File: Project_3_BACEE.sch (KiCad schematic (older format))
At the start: 16 parts

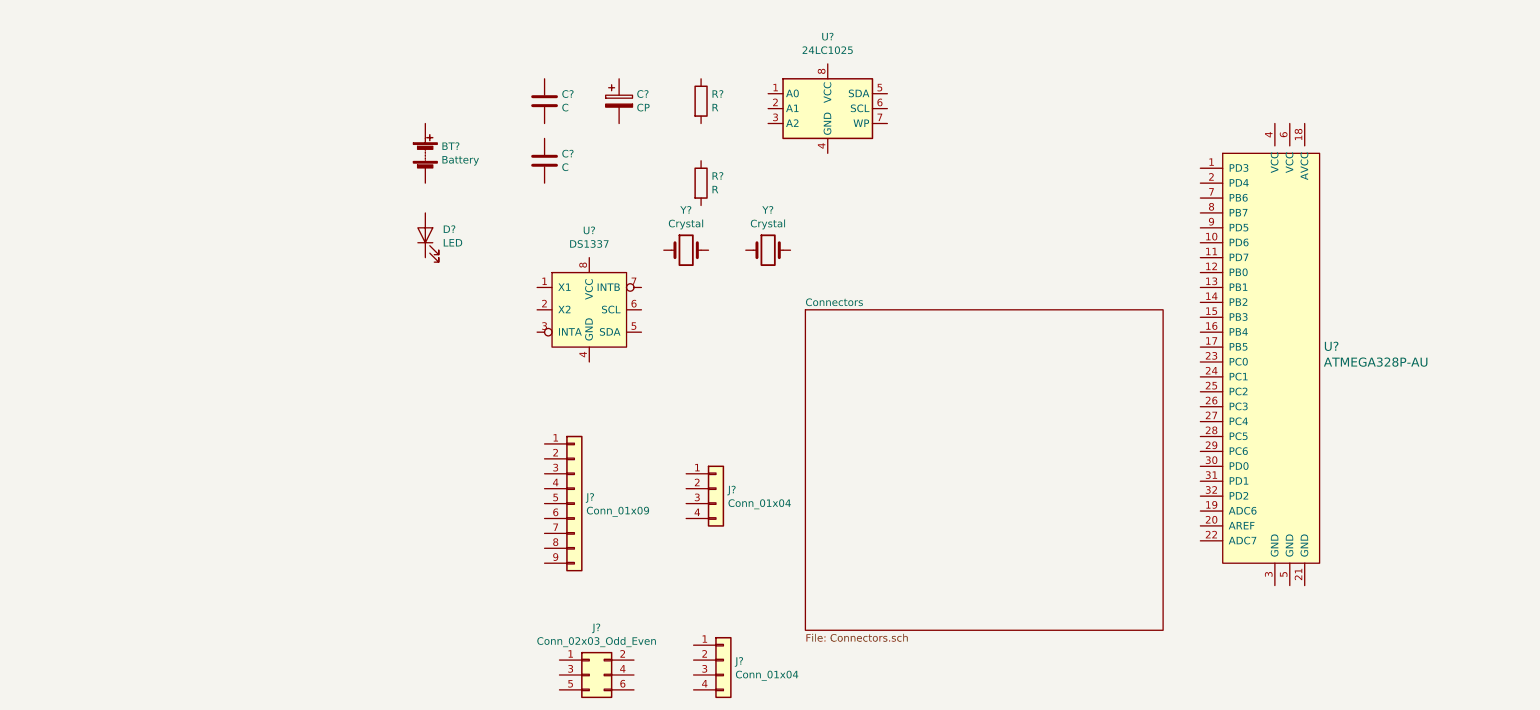
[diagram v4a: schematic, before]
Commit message: Arranged symbols.
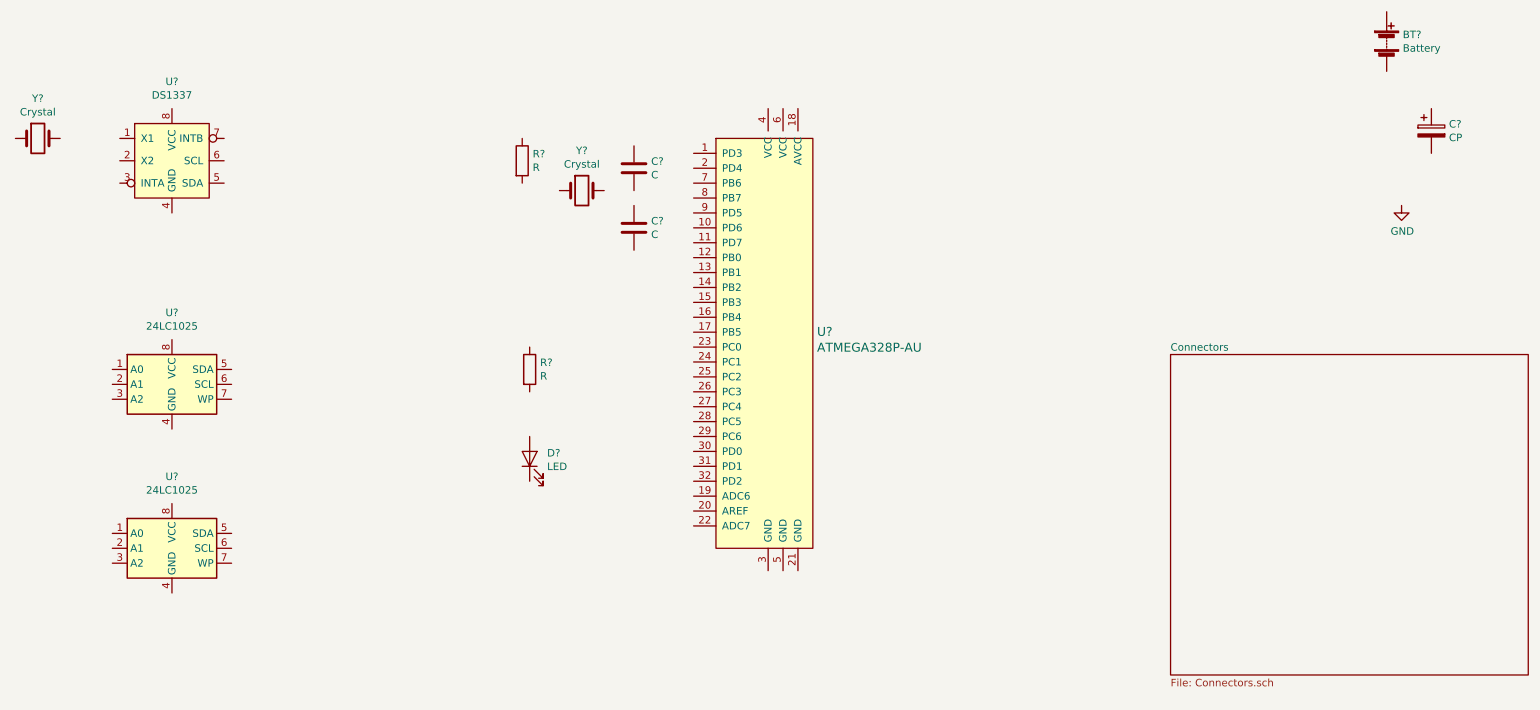
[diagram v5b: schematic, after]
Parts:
- removed J?: Conn_01x09, symbol Connector_Generic:Conn_01x09
- removed J? (x2): Conn_01x04, symbol Connector_Generic:Conn_01x04
- removed J?: Conn_02x03_Odd_Even, symbol Connector_Generic:Conn_02x03_Odd_Even
- added U?: 24LC1025, symbol Memory_EEPROM:24LC1025
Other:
- moved on the sheet: BT?, C?, D?, R?, U?, Y?
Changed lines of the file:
@@
 L Device:Battery BT?
 U 1 1 5D8368FA
-P 3700 2550
-F 0 "BT?" H 3808 2596 50  0000 L CNN
-F 1 "Battery" H 3808 2505 50  0000 L CNN
-F 2 "" V 3700 2610 50  0001 C CNN
-F 3 "~" V 3700 2610 50  0001 C CNN
-	1    3700 2550
+P 10150 1800
+F 0 "BT?" H 10258 1846 50  0000 L CNN
+F 1 "Battery" H 10258 1755 50  0000 L CNN
+F 2 "" V 10150 1860 50  0001 C CNN
+F 3 "~" V 10150 1860 50  0001 C CNN
+	1    10150 1800
 	1    0    0    -1
 $EndComp
@@
 L Device:C C?
 U 1 1 5D837139
-P 4500 2200
-F 0 "C?" H 4615 2246 50  0000 L CNN
-F 1 "C" H 4615 2155 50  0000 L CNN
-F 2 "" H 4538 2050 50  0001 C CNN
-F 3 "~" H 4500 2200 50  0001 C CNN
-	1    4500 2200
+P 5100 2650
+F 0 "C?" H 5215 2696 50  0000 L CNN
+F 1 "C" H 5215 2605 50  0000 L CNN
+F 2 "" H 5138 2500 50  0001 C CNN
+F 3 "~" H 5100 2650 50  0001 C CNN
+	1    5100 2650
 	1    0    0    -1
 $EndComp
@@
 L Device:C C?
 U 1 1 5D837758
-P 4500 2600
-F 0 "C?" H 4615 2646 50  0000 L CNN
-F 1 "C" H 4615 2555 50  0000 L CNN
-F 2 "" H 4538 2450 50  0001 C CNN
-F 3 "~" H 4500 2600 50  0001 C CNN
-	1    4500 2600
+P 5100 3050
+F 0 "C?" H 5215 3096 50  0000 L CNN
+F 1 "C" H 5215 3005 50  0000 L CNN
+F 2 "" H 5138 2900 50  0001 C CNN
+F 3 "~" H 5100 3050 50  0001 C CNN
+	1    5100 3050
 	1    0    0    -1
 $EndComp
@@
 L Device:CP C?
 U 1 1 5D837C3D
-P 5000 2200
-F 0 "C?" H 5118 2246 50  0000 L CNN
-F 1 "CP" H 5118 2155 50  0000 L CNN
-F 2 "" H 5038 2050 50  0001 C CNN
-F 3 "~" H 5000 2200 50  0001 C CNN
-	1    5000 2200
+P 10450 2400
+F 0 "C?" H 10568 2446 50  0000 L CNN
+F 1 "CP" H 10568 2355 50  0000 L CNN
+F 2 "" H 10488 2250 50  0001 C CNN
+F 3 "~" H 10450 2400 50  0001 C CNN
+	1    10450 2400
 	1    0    0    -1
 $EndComp
@@
 L Device:LED D?
 U 1 1 5D8380C0
-P 3700 3100
-F 0 "D?" V 3739 2983 50  0000 R CNN
-F 1 "LED" V 3648 2983 50  0000 R CNN
-F 2 "" H 3700 3100 50  0001 C CNN
-F 3 "~" H 3700 3100 50  0001 C CNN
-	1    3700 3100
+P 4400 4600
+F 0 "D?" V 4439 4483 50  0000 R CNN
+F 1 "LED" V 4348 4483 50  0000 R CNN
+F 2 "" H 4400 4600 50  0001 C CNN
+F 3 "~" H 4400 4600 50  0001 C CNN
+	1    4400 4600
 	0    -1   -1   0
 $EndComp
@@
 L Device:R R?
 U 1 1 5D8396B9
-P 5550 2200
-F 0 "R?" H 5620 2246 50  0000 L CNN
-F 1 "R" H 5620 2155 50  0000 L CNN
-F 2 "" V 5480 2200 50  0001 C CNN
-F 3 "~" H 5550 2200 50  0001 C CNN
-	1    5550 2200
+P 4350 2600
+F 0 "R?" H 4420 2646 50  0000 L CNN
+F 1 "R" H 4420 2555 50  0000 L CNN
+F 2 "" V 4280 2600 50  0001 C CNN
+F 3 "~" H 4350 2600 50  0001 C CNN
+	1    4350 2600
 	1    0    0    -1
 $EndComp
@@
 L Device:R R?
 U 1 1 5D839B71
-P 5550 2750
-F 0 "R?" H 5620 2796 50  0000 L CNN
-F 1 "R" H 5620 2705 50  0000 L CNN
-F 2 "" V 5480 2750 50  0001 C CNN
-F 3 "~" H 5550 2750 50  0001 C CNN
-	1    5550 2750
+P 4400 4000
+F 0 "R?" H 4470 4046 50  0000 L CNN
+F 1 "R" H 4470 3955 50  0000 L CNN
+F 2 "" V 4330 4000 50  0001 C CNN
+F 3 "~" H 4400 4000 50  0001 C CNN
+	1    4400 4000
 	1    0    0    -1
 $EndComp
@@
 L Memory_EEPROM:24LC1025 U?
 U 1 1 5D83A291
-P 6400 2250
-F 0 "U?" H 6400 2731 50  0000 C CNN
-F 1 "24LC1025" H 6400 2640 50  0000 C CNN
-F 2 "" H 6400 2250 50  0001 C CNN
-F 3 "http://ww1.microchip.com/downloads/en/DeviceDoc/21941B.pdf" H 6400 2250 50  0001 C CNN
-	1    6400 2250
+P 2000 4100
+F 0 "U?" H 2000 4581 50  0000 C CNN
+F 1 "24LC1025" H 2000 4490 50  0000 C CNN
+F 2 "" H 2000 4100 50  0001 C CNN
+F 3 "http://ww1.microchip.com/downloads/en/DeviceDoc/21941B.pdf" H 2000 4100 50  0001 C CNN
+	1    2000 4100
 	1    0    0    -1
 $EndComp
 $Sheet
-S 6250 3600 2400 2150
+S 8700 3900 2400 2150
 U 5D83B0D5
 F0 "Connectors" 50
@@
 $EndSheet
 $Comp
-L Connector_Generic:Conn_01x09 J?
-U 1 1 5D83BD36
-P 4700 4900
-F 0 "J?" H 4780 4942 50  0000 L CNN
-F 1 "Conn_01x09" H 4780 4851 50  0000 L CNN
-F 2 "" H 4700 4900 50  0001 C CNN
-F 3 "~" H 4700 4900 50  0001 C CNN
-	1    4700 4900
-	1    0    0    -1
-$EndComp
-$Comp
-L Connector_Generic:Conn_01x04 J?
-U 1 1 5D83CD16
-P 5650 4800
-F 0 "J?" H 5730 4792 50  0000 L CNN
-F 1 "Conn_01x04" H 5730 4701 50  0000 L CNN
-F 2 "" H 5650 4800 50  0001 C CNN
-F 3 "~" H 5650 4800 50  0001 C CNN
-	1    5650 4800
-	1    0    0    -1
-$EndComp
-$Comp
-L Connector_Generic:Conn_02x03_Odd_Even J?
-U 1 1 5D83D5F4
-P 4800 6050
-F 0 "J?" H 4850 6367 50  0000 C CNN
-F 1 "Conn_02x03_Odd_Even" H 4850 6276 50  0000 C CNN
-F 2 "" H 4800 6050 50  0001 C CNN
-F 3 "~" H 4800 6050 50  0001 C CNN
-	1    4800 6050
-	1    0    0    -1
-$EndComp
-$Comp
-L Connector_Generic:Conn_01x04 J?
-U 1 1 5D83E499
-P 5700 5950
-F 0 "J?" H 5780 5942 50  0000 L CNN
-F 1 "Conn_01x04" H 5780 5851 50  0000 L CNN
-F 2 "" H 5700 5950 50  0001 C CNN
-F 3 "~" H 5700 5950 50  0001 C CNN
-	1    5700 5950
-	1    0    0    -1
-$EndComp
-$Comp
 L dk_Embedded-Microcontrollers:ATMEGA328P-AU U?
 U 1 1 5D839D67
-P 9400 3950
-F 0 "U?" H 9728 4053 60  0000 L CNN
-F 1 "ATMEGA328P-AU" H 9728 3947 60  0000 L CNN
-F 2 "digikey-footprints:TQFP-32_7x7mm" H 9600 4150 60  0001 L CNN
-F 3 "http://www.microchip.com/mymicrochip/filehandler.aspx?ddocname=en608326" H 9600 4250 60  0001 L CNN
-F 4 "ATMEGA328P-AU-ND" H 9600 4350 60  0001 L CNN "Digi-Key_PN"
-F 5 "ATMEGA328P-AU" H 9600 4450 60  0001 L CNN "MPN"
-F 6 "Integrated Circuits (ICs)" H 9600 4550 60  0001 L CNN "Category"
-F 7 "Embedded - Microcontrollers" H 9600 4650 60  0001 L CNN "Family"
-F 8 "http://www.microchip.com/mymicrochip/filehandler.aspx?ddocname=en608326" H 9600 4750 60  0001 L CNN "DK_Datasheet_Link"
-F 9 "/product-detail/en/microchip-technology/ATMEGA328P-AU/ATMEGA328P-AU-ND/1832260" H 9600 4850 60  0001 L CNN "DK_Detail_Page"
-F 10 "IC MCU 8BIT 32KB FLASH 32TQFP" H 9600 4950 60  0001 L CNN "Description"
-F 11 "Microchip Technology" H 9600 5050 60  0001 L CNN "Manufacturer"
-F 12 "Active" H 9600 5150 60  0001 L CNN "Status"
-	1    9400 3950
+P 6000 3850
+F 0 "U?" H 6328 3953 60  0000 L CNN
+F 1 "ATMEGA328P-AU" H 6328 3847 60  0000 L CNN
+F 2 "digikey-footprints:TQFP-32_7x7mm" H 6200 4050 60  0001 L CNN
+F 3 "http://www.microchip.com/mymicrochip/filehandler.aspx?ddocname=en608326" H 6200 4150 60  0001 L CNN
+F 4 "ATMEGA328P-AU-ND" H 6200 4250 60  0001 L CNN "Digi-Key_PN"
+F 5 "ATMEGA328P-AU" H 6200 4350 60  0001 L CNN "MPN"
+F 6 "Integrated Circuits (ICs)" H 6200 4450 60  0001 L CNN "Category"
+F 7 "Embedded - Microcontrollers" H 6200 4550 60  0001 L CNN "Family"
+F 8 "http://www.microchip.com/mymicrochip/filehandler.aspx?ddocname=en608326" H 6200 4650 60  0001 L CNN "DK_Datasheet_Link"
+F 9 "/product-detail/en/microchip-technology/ATMEGA328P-AU/ATMEGA328P-AU-ND/1832260" H 6200 4750 60  0001 L CNN "DK_Detail_Page"
+F 10 "IC MCU 8BIT 32KB FLASH 32TQFP" H 6200 4850 60  0001 L CNN "Description"
+F 11 "Microchip Technology" H 6200 4950 60  0001 L CNN "Manufacturer"
+F 12 "Active" H 6200 5050 60  0001 L CNN "Status"
+	1    6000 3850
 	1    0    0    -1
 $EndComp
@@
 L Real_Time_Clock:DS1337 U?
 U 1 1 5D83D55D
-P 4800 3600
-F 0 "U?" H 4800 4131 50  0000 C CNN
-F 1 "DS1337" H 4800 4040 50  0000 C CNN
-F 2 "" H 5050 4350 50  0001 C CNN
-F 3 "http://www.farnell.com/datasheets/2000844.pdf?_ga=2.177508589.917776798.1568905288-909876714.1550950510&_gac=1.216414692.1568905288.Cj0KCQjwzozsBRCNARIsAEM9kBOgoySVZbm8O6iFhnJvaEFTPgnKihPjdqZAtUZmWq1n3gbdbDGyVXUaAgFCEALw_wcB" H 5050 4350 50  0001 C CNN
-	1    4800 3600
+P 2000 2600
+F 0 "U?" H 2000 3131 50  0000 C CNN
+F 1 "DS1337" H 2000 3040 50  0000 C CNN
+F 2 "" H 2250 3350 50  0001 C CNN
+F 3 "http://www.farnell.com/datasheets/2000844.pdf?_ga=2.177508589.917776798.1568905288-909876714.1550950510&_gac=1.216414692.1568905288.Cj0KCQjwzozsBRCNARIsAEM9kBOgoySVZbm8O6iFhnJvaEFTPgnKihPjdqZAtUZmWq1n3gbdbDGyVXUaAgFCEALw_wcB" H 2250 3350 50  0001 C CNN
+	1    2000 2600
 	1    0    0    -1
 $EndComp
@@
 L Device:Crystal Y?
 U 1 1 5D83E063
-P 5450 3200
-F 0 "Y?" H 5450 3468 50  0000 C CNN
-F 1 "Crystal" H 5450 3377 50  0000 C CNN
-F 2 "" H 5450 3200 50  0001 C CNN
-F 3 "~" H 5450 3200 50  0001 C CNN
-	1    5450 3200
+P 1100 2450
+F 0 "Y?" H 1100 2718 50  0000 C CNN
+F 1 "Crystal" H 1100 2627 50  0000 C CNN
+F 2 "" H 1100 2450 50  0001 C CNN
+F 3 "~" H 1100 2450 50  0001 C CNN
+	1    1100 2450
 	1    0    0    -1
 $EndComp
@@
 L Device:Crystal Y?
 U 1 1 5D83E859
-P 6000 3200
-F 0 "Y?" H 6000 3468 50  0000 C CNN
-F 1 "Crystal" H 6000 3377 50  0000 C CNN
-F 2 "" H 6000 3200 50  0001 C CNN
-F 3 "~" H 6000 3200 50  0001 C CNN
-	1    6000 3200
+P 4750 2800
+F 0 "Y?" H 4750 3068 50  0000 C CNN
+F 1 "Crystal" H 4750 2977 50  0000 C CNN
+F 2 "" H 4750 2800 50  0001 C CNN
+F 3 "~" H 4750 2800 50  0001 C CNN
+	1    4750 2800
 	1    0    0    -1
 $EndComp
+$Comp
+L Memory_EEPROM:24LC1025 U?
+U 1 1 5D841166
+P 2000 5200
+F 0 "U?" H 2000 5681 50  0000 C CNN
+F 1 "24LC1025" H 2000 5590 50  0000 C CNN
+F 2 "" H 2000 5200 50  0001 C CNN
+F 3 "http://ww1.microchip.com/downloads/en/DeviceDoc/21941B.pdf" H 2000 5200 50  0001 C CNN
+	1    2000 5200
+	1    0    0    -1
+$EndComp
+$Comp
+L power:GND #PWR?
+U 1 1 5D84B27E
+P 10250 2900
+F 0 "#PWR?" H 10250 2650 50  0001 C CNN
+F 1 "GND" H 10255 2727 50  0000 C CNN
+F 2 "" H 10250 2900 50  0001 C CNN
+F 3 "" H 10250 2900 50  0001 C CNN
+	1    10250 2900
+	1    0    0    -1
+$EndComp

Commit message: Anottated.
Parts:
- gave numbers to parts that had none: 13
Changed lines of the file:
@@
 $EndDescr
 $Comp
-L Device:Battery BT?
+L Device:Battery BT1
 U 1 1 5D8368FA
 P 10150 1800
-F 0 "BT?" H 10258 1846 50  0000 L CNN
+F 0 "BT1" H 10258 1846 50  0000 L CNN
 F 1 "Battery" H 10258 1755 50  0000 L CNN
 F 2 "" V 10150 1860 50  0001 C CNN
@@
 $EndComp
 $Comp
-L Device:C C?
+L Device:C C1
 U 1 1 5D837139
 P 5100 2650
-F 0 "C?" H 5215 2696 50  0000 L CNN
+F 0 "C1" H 5215 2696 50  0000 L CNN
 F 1 "C" H 5215 2605 50  0000 L CNN
 F 2 "" H 5138 2500 50  0001 C CNN
@@
 $EndComp
 $Comp
-L Device:C C?
+L Device:C C2
 U 1 1 5D837758
 P 5100 3050
-F 0 "C?" H 5215 3096 50  0000 L CNN
+F 0 "C2" H 5215 3096 50  0000 L CNN
 F 1 "C" H 5215 3005 50  0000 L CNN
 F 2 "" H 5138 2900 50  0001 C CNN
@@
 $EndComp
 $Comp
-L Device:CP C?
+L Device:CP C3
 U 1 1 5D837C3D
 P 10450 2400
-F 0 "C?" H 10568 2446 50  0000 L CNN
+F 0 "C3" H 10568 2446 50  0000 L CNN
 F 1 "CP" H 10568 2355 50  0000 L CNN
 F 2 "" H 10488 2250 50  0001 C CNN
@@
 $EndComp
 $Comp
-L Device:LED D?
+L Device:LED D1
 U 1 1 5D8380C0
 P 4400 4600
-F 0 "D?" V 4439 4483 50  0000 R CNN
+F 0 "D1" V 4439 4483 50  0000 R CNN
 F 1 "LED" V 4348 4483 50  0000 R CNN
 F 2 "" H 4400 4600 50  0001 C CNN
@@
 $EndComp
 $Comp
-L Device:R R?
+L Device:R R1
 U 1 1 5D8396B9
 P 4350 2600
-F 0 "R?" H 4420 2646 50  0000 L CNN
+F 0 "R1" H 4420 2646 50  0000 L CNN
 F 1 "R" H 4420 2555 50  0000 L CNN
 F 2 "" V 4280 2600 50  0001 C CNN
@@
 $EndComp
 $Comp
-L Device:R R?
+L Device:R R2
 U 1 1 5D839B71
 P 4400 4000
-F 0 "R?" H 4470 4046 50  0000 L CNN
+F 0 "R2" H 4470 4046 50  0000 L CNN
 F 1 "R" H 4470 3955 50  0000 L CNN
 F 2 "" V 4330 4000 50  0001 C CNN
@@
 $EndComp
 $Comp
-L Memory_EEPROM:24LC1025 U?
+L Memory_EEPROM:24LC1025 U2
 U 1 1 5D83A291
 P 2000 4100
-F 0 "U?" H 2000 4581 50  0000 C CNN
+F 0 "U2" H 2000 4581 50  0000 C CNN
 F 1 "24LC1025" H 2000 4490 50  0000 C CNN
 F 2 "" H 2000 4100 50  0001 C CNN
@@
 $EndSheet
 $Comp
-L dk_Embedded-Microcontrollers:ATMEGA328P-AU U?
+L dk_Embedded-Microcontrollers:ATMEGA328P-AU U4
 U 1 1 5D839D67
 P 6000 3850
-F 0 "U?" H 6328 3953 60  0000 L CNN
+F 0 "U4" H 6328 3953 60  0000 L CNN
 F 1 "ATMEGA328P-AU" H 6328 3847 60  0000 L CNN
 F 2 "digikey-footprints:TQFP-32_7x7mm" H 6200 4050 60  0001 L CNN
@@
 $EndComp
 $Comp
-L Real_Time_Clock:DS1337 U?
+L Real_Time_Clock:DS1337 U1
 U 1 1 5D83D55D
 P 2000 2600
-F 0 "U?" H 2000 3131 50  0000 C CNN
+F 0 "U1" H 2000 3131 50  0000 C CNN
 F 1 "DS1337" H 2000 3040 50  0000 C CNN
 F 2 "" H 2250 3350 50  0001 C CNN
@@
 $EndComp
 $Comp
-L Device:Crystal Y?
+L Device:Crystal Y1
 U 1 1 5D83E063
 P 1100 2450
-F 0 "Y?" H 1100 2718 50  0000 C CNN
+F 0 "Y1" H 1100 2718 50  0000 C CNN
 F 1 "Crystal" H 1100 2627 50  0000 C CNN
 F 2 "" H 1100 2450 50  0001 C CNN
@@
 $EndComp
 $Comp
-L Device:Crystal Y?
+L Device:Crystal Y2
 U 1 1 5D83E859
 P 4750 2800
-F 0 "Y?" H 4750 3068 50  0000 C CNN
+F 0 "Y2" H 4750 3068 50  0000 C CNN
 F 1 "Crystal" H 4750 2977 50  0000 C CNN
 F 2 "" H 4750 2800 50  0001 C CNN
@@
 $EndComp
 $Comp
-L Memory_EEPROM:24LC1025 U?
+L Memory_EEPROM:24LC1025 U3
 U 1 1 5D841166
 P 2000 5200
-F 0 "U?" H 2000 5681 50  0000 C CNN
+F 0 "U3" H 2000 5681 50  0000 C CNN
 F 1 "24LC1025" H 2000 5590 50  0000 C CNN
 F 2 "" H 2000 5200 50  0001 C CNN
@@
 $EndComp
 $Comp
-L power:GND #PWR?
+L power:GND #PWR01
 U 1 1 5D84B27E
 P 10250 2900
-F 0 "#PWR?" H 10250 2650 50  0001 C CNN
+F 0 "#PWR01" H 10250 2650 50  0001 C CNN
 F 1 "GND" H 10255 2727 50  0000 C CNN
 F 2 "" H 10250 2900 50  0001 C CNN
